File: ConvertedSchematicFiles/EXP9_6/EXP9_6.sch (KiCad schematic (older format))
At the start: 8 parts, among them U1 74393

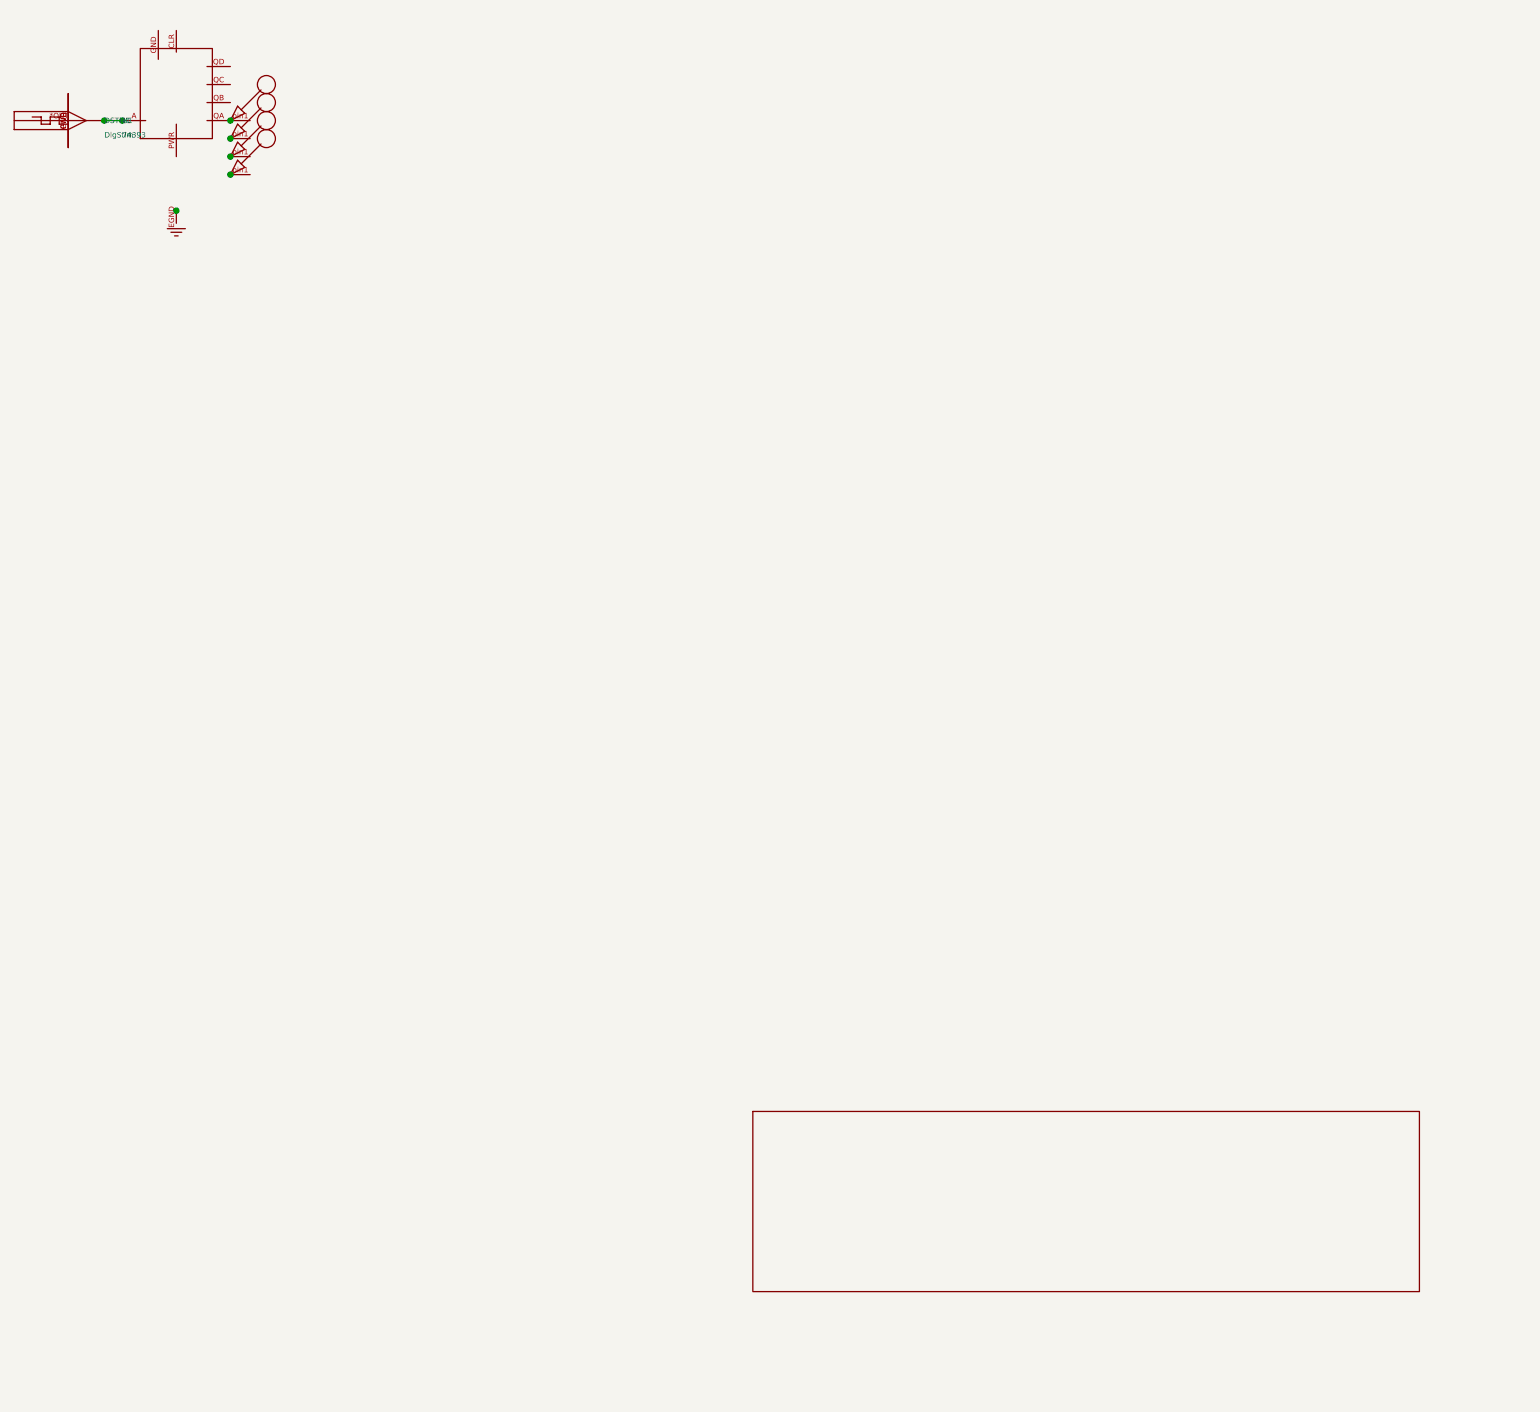
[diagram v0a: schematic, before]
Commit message: Excluded some components. These no longer appear after conversion. When calling shell commands, filenames are in "quotes"
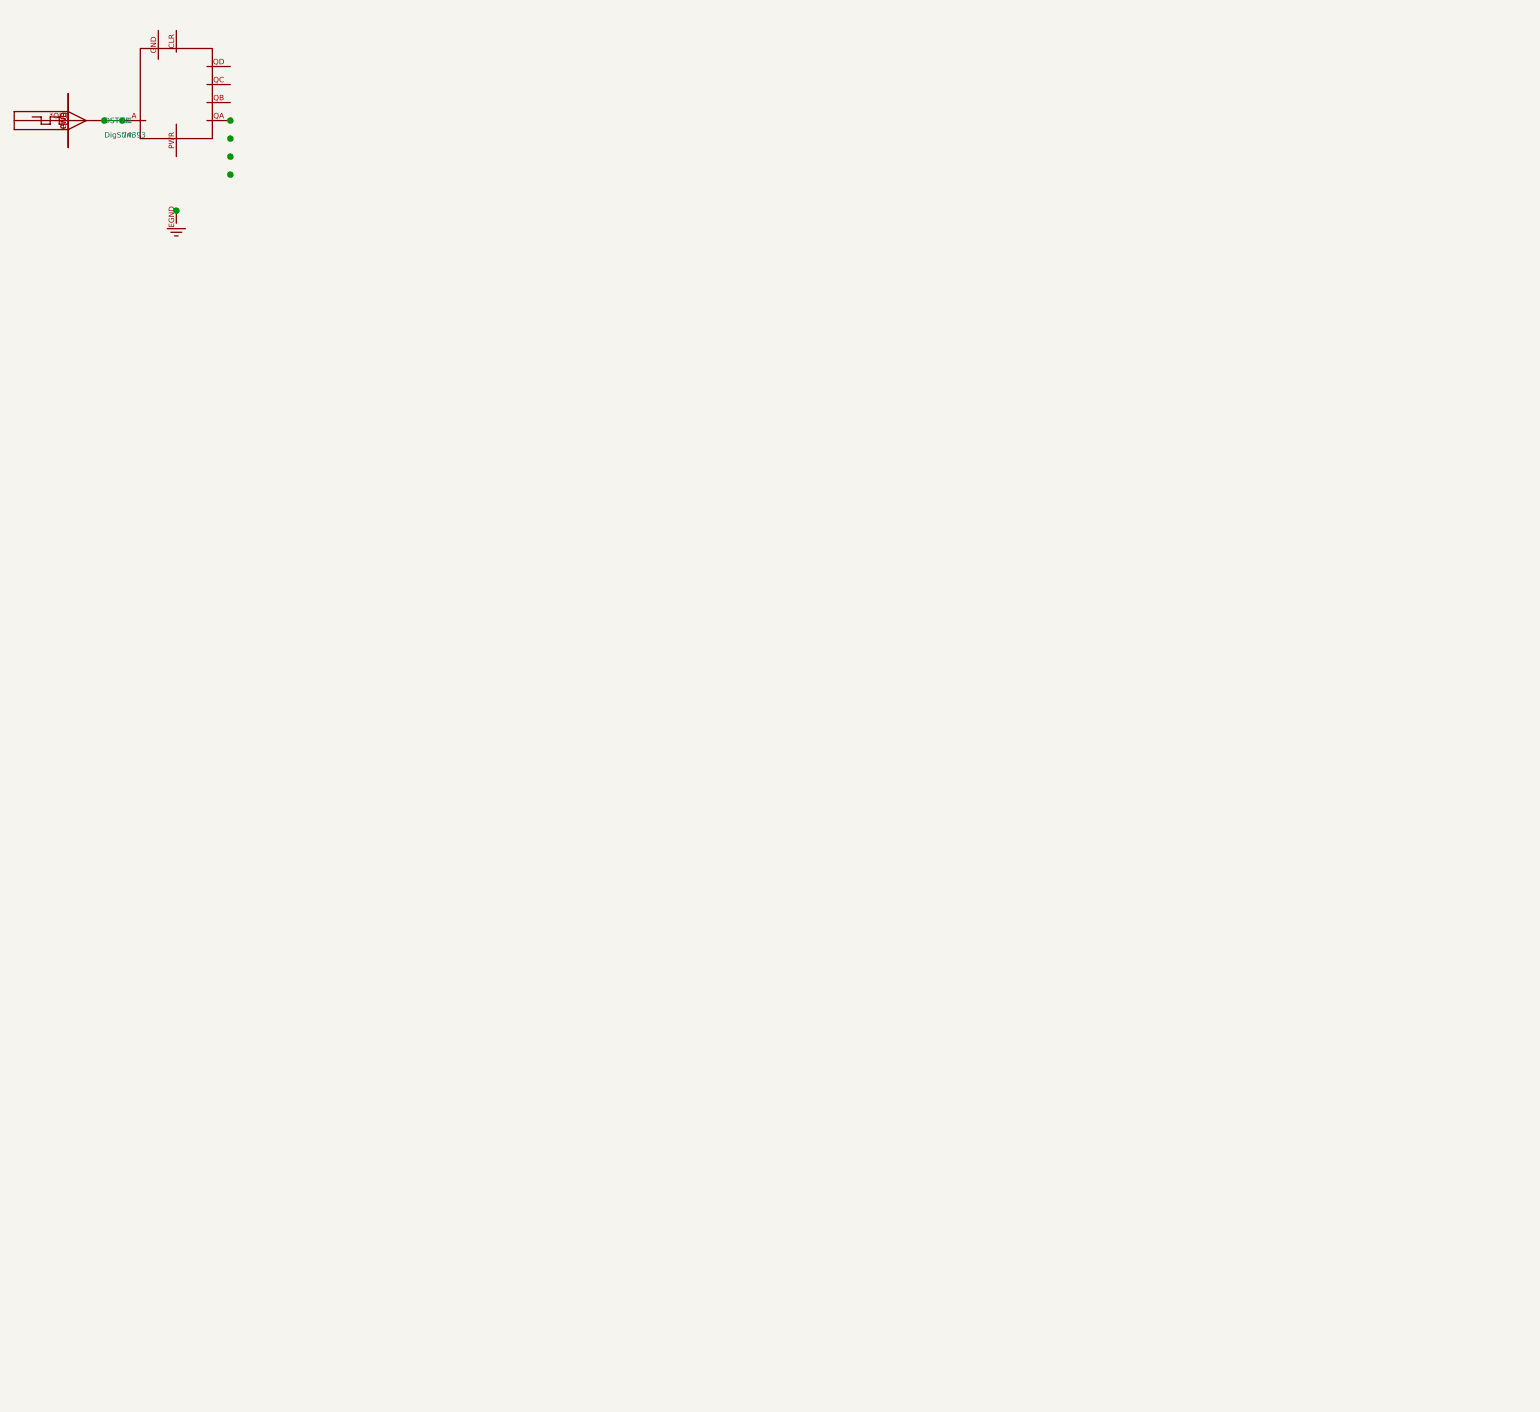
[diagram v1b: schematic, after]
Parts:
- removed nodeMarker (x4): nodeMarker, symbol NODEMARKER_PSPICE
- removed titleblk: titleblk, symbol TITLEBLK_PSPICE
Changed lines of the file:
@@
-	1    0    0    1
-$EndComp
-$Comp
-L TITLEBLK_PSPICE titleblk
-U 1 1 14636915
-P 9700 7200
-F 0 "titleblk" H 19400 14400 30  0001 L CNN
-F 1 "titleblk" H 19400 14480 30  0001 L CNN
-	1    9700 7200
-	1    0    0    1
-$EndComp
-$Comp
-L NODEMARKER_PSPICE nodeMarker
-U 1 1 77747793
-P 3100 900
-F 0 "nodeMarker" H 6200 1800 30  0001 L CNN
-F 1 "nodeMarker" H 6200 1880 30  0001 L CNN
-	1    3100 900
-	1    0    0    1
-$EndComp
-$Comp
-L NODEMARKER_PSPICE nodeMarker
-U 1 1 74238335
-P 3100 1000
-F 0 "nodeMarker" H 6200 2000 30  0001 L CNN
-F 1 "nodeMarker" H 6200 2080 30  0001 L CNN
-	1    3100 1000
-	1    0    0    1
-$EndComp
-$Comp
-L NODEMARKER_PSPICE nodeMarker
-U 1 1 99885386
-P 3100 800
-F 0 "nodeMarker" H 6200 1600 30  0001 L CNN
-F 1 "nodeMarker" H 6200 1680 30  0001 L CNN
-	1    3100 800
-	1    0    0    1
-$EndComp
-$Comp
-L NODEMARKER_PSPICE nodeMarker
-U 1 1 39760492
-P 3100 700
-F 0 "nodeMarker" H 6200 1400 30  0001 L CNN
-F 1 "nodeMarker" H 6200 1480 30  0001 L CNN
-	1    3100 700
 	1    0    0    1
 $EndComp

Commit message: Ports issue fixed. Now annotation for ports is #PWR? function added "itos"
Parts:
- removed EGND: EGND, symbol EGND_PSPICE
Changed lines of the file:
@@
 $EndDescr
 $Comp
-L EGND_PSPICE EGND
+L EGND_PSPICE #PWR1
 U 1 1 14289383
 P 2800 1200
-F 0 "EGND" H 5600 2400 30  0001 L CNN
+F 0 "#PWR1" H 5600 2400 30  0001 L CNN
 F 1 "EGND" H 5600 2480 30  0001 L CNN
 	1    2800 1200

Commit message: Added LICENSE.txt
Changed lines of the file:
@@
 $EndDescr
 $Comp
-L EGND_PSPICE #PWR1
+L GND #PWR1
 U 1 1 14289383
 P 2800 1200

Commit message: Orientation fix. Library components are now inverted, with +ve y axis going up. In Schematic files, +ve y axis is downwards. This is how the KiCad libraries are. As a result of the above fixed, the converted GND is now oriented correctly.
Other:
- moved on the sheet: U1
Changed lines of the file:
@@
 F 1 "EGND" H 5600 2480 30  0001 L CNN
 	1    2800 1200
-	1    0    0    1
+	1    0    0    -1
 $EndComp
 $Comp
@@
 F 1 "DigStim" H 2400 780 30  0000 L CNN
 	1    2400 700
-	1    0    0    1
+	1    0    0    -1
 $EndComp
 $Comp
@@
 F 1 "74393" H 2500 780 30  0000 L CNN
 	1    2500 700
-	1    0    0    1
+	1    0    0    -1
 $EndComp
 Wire Wire Line

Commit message: Removed the use of exec, wrote basename function, made integration with eSim easier.
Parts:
- added nodeMarker (x4): nodeMarker, symbol nodeMarker_PSPICE
- added titleblk: titleblk, symbol titleblk_PSPICE
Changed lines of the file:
@@
-EESchema Schematic File Version 2  date Monday 28 February 2000 08:23:25 PM IST
+EESchema Schematic File Version 2  date
 LIBS:power
 LIBS:device
@@
 LIBS:contrib
 LIBS:valves
-LIBS:ConvertedSchematicFiles/EXP9_6-cache
 EELAYER 25  0
 EELAYER END
@@
 Sheet 1 1
 Title ""
-Date "28 Feb 2000"
+Date ""
 Rev ""
 Comp ""
@@
 	1    0    0    -1
 $EndComp
+$Comp
+L titleblk_PSPICE titleblk
+U 1 1 14636915
+P 9700 7200
+F 0 "titleblk" H 19400 14400 30  0001 L CNN
+F 1 "titleblk" H 19400 14480 30  0001 L CNN
+	1    9700 7200
+	1    0    0    -1
+$EndComp
+$Comp
+L nodeMarker_PSPICE nodeMarker
+U 1 1 77747793
+P 3100 900
+F 0 "nodeMarker" H 6200 1800 30  0001 L CNN
+F 1 "nodeMarker" H 6200 1880 30  0001 L CNN
+	1    3100 900
+	1    0    0    -1
+$EndComp
+$Comp
+L nodeMarker_PSPICE nodeMarker
+U 1 1 74238335
+P 3100 1000
+F 0 "nodeMarker" H 6200 2000 30  0001 L CNN
+F 1 "nodeMarker" H 6200 2080 30  0001 L CNN
+	1    3100 1000
+	1    0    0    -1
+$EndComp
+$Comp
+L nodeMarker_PSPICE nodeMarker
+U 1 1 99885386
+P 3100 800
+F 0 "nodeMarker" H 6200 1600 30  0001 L CNN
+F 1 "nodeMarker" H 6200 1680 30  0001 L CNN
+	1    3100 800
+	1    0    0    -1
+$EndComp
+$Comp
+L nodeMarker_PSPICE nodeMarker
+U 1 1 39760492
+P 3100 700
+F 0 "nodeMarker" H 6200 1400 30  0001 L CNN
+F 1 "nodeMarker" H 6200 1480 30  0001 L CNN
+	1    3100 700
+	1    0    0    -1
+$EndComp
